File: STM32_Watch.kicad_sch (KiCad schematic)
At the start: 50 parts, among them Q1 AO3401A, SW1 SW_Push, SW2 SW_Push, U1 STM32L031K6Ux, U2 LIS2MDL, X1 32.768k

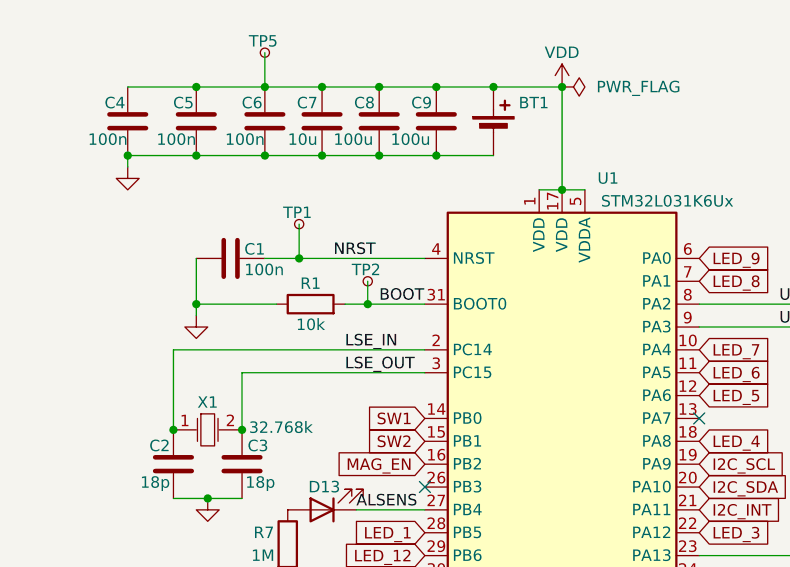
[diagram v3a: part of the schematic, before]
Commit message: Realigned components & Removed boot TP
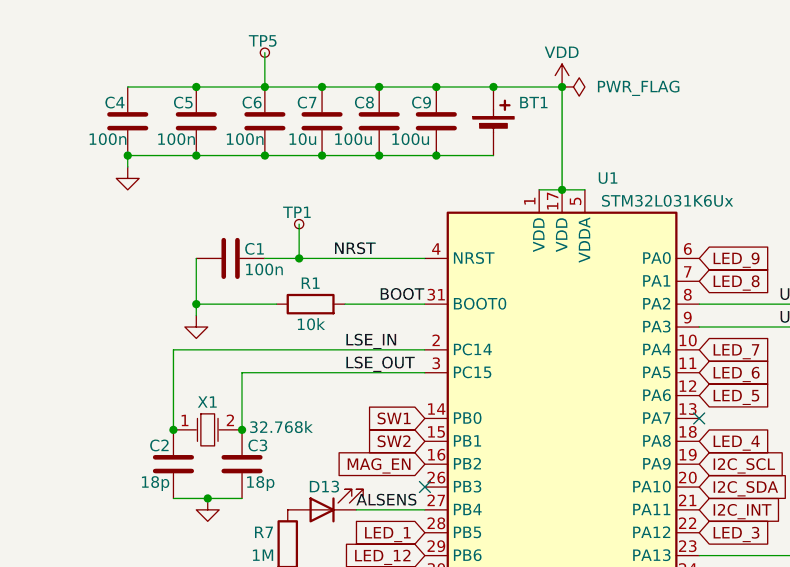
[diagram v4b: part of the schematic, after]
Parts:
- removed TP2: TestPoint_Small, TestPoint:TestPoint_Pad_D1.0mm, symbol Connector:TestPoint_Small
- TP1, TP3, TP4, TP5, TP6, TP7, TP8: footprint TestPoint:TestPoint_Pad_D1.0mm -> TestPoint:TestPoint_Pad_D1.5mm
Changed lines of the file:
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@@
 	)
 	(junction
-		(at 71.12 58.42)
-		(diameter 0)
-		(color 0 0 0 0)
-	)
-	(junction
 		(at 97.79 182.88)
 		(diameter 0)
@@
 	(wire
 		(pts
-			(xy 68.58 58.42) (xy 71.12 58.42)
-		)
-		(stroke
-			(width 0)
-			(type default)
-		)
-	)
-	(wire
-		(pts
 			(xy 101.6 154.94) (xy 106.68 154.94)
 		)
@@
 	(wire
 		(pts
-			(xy 71.12 55.88) (xy 71.12 58.42)
-		)
-		(stroke
-			(width 0)
-			(type default)
-		)
-	)
-	(wire
-		(pts
 			(xy 57.15 66.04) (xy 57.15 72.39)
 		)
@@
 	(wire
 		(pts
-			(xy 71.12 58.42) (xy 77.47 58.42)
+			(xy 68.58 58.42) (xy 77.47 58.42)
 		)
 		(stroke
@@
 			)
 		)
-		(property "Footprint" "TestPoint:TestPoint_Pad_D1.0mm"
+		(property "Footprint" "TestPoint:TestPoint_Pad_D1.5mm"
 			(at 130.81 58.42 0)
 			(effects
@@
 	)
 	(symbol
-		(lib_id "Connector:TestPoint_Small")
-		(at 71.12 55.88 0)
-		(unit 1)
-		(exclude_from_sim no)
-		(in_bom yes)
-		(on_board yes)
-		(dnp no)
-		(property "Reference" "TP2"
-			(at 69.342 54.61 0)
-			(effects
-				(font
-					(size 1.27 1.27)
-				)
-				(justify left)
-			)
-		)
-		(property "Value" "TestPoint_Small"
-			(at 72.39 57.1499 0)
-			(effects
-				(font
-					(size 1.27 1.27)
-				)
-				(justify left)
-				(hide yes)
-			)
-		)
-		(property "Footprint" "TestPoint:TestPoint_Pad_D1.0mm"
-			(at 76.2 55.88 0)
-			(effects
-				(font
-					(size 1.27 1.27)
-				)
-				(hide yes)
-			)
-		)
-		(property "Datasheet" "~"
-			(at 76.2 55.88 0)
-			(effects
-				(font
-					(size 1.27 1.27)
-				)
-				(hide yes)
-			)
-		)
-		(property "Description" "test point"
-			(at 71.12 55.88 0)
-			(effects
-				(font
-					(size 1.27 1.27)
-				)
-				(hide yes)
-			)
-		)
-		(pin "1"
-		)
-		(instances
-			(project "STM32_Watch"
-				(path "/1b502511-4b9c-43d1-bc6f-3ad66e0f6a7c"
-					(reference "TP2")
-					(unit 1)
-				)
-			)
-		)
-	)
-	(symbol
 		(lib_id "power:GND")
 		(at 92.71 101.6 0)
@@
 			)
 		)
-		(property "Footprint" "TestPoint:TestPoint_Pad_D1.0mm"
+		(property "Footprint" "TestPoint:TestPoint_Pad_D1.5mm"
 			(at 130.81 88.9 0)
 			(effects
@@
 			)
 		)
-		(property "Footprint" "TestPoint:TestPoint_Pad_D1.0mm"
+		(property "Footprint" "TestPoint:TestPoint_Pad_D1.5mm"
 			(at 130.81 86.36 0)
 			(effects
@@
 			)
 		)
-		(property "Footprint" "TestPoint:TestPoint_Pad_D1.0mm"
+		(property "Footprint" "TestPoint:TestPoint_Pad_D1.5mm"
 			(at 130.81 60.96 0)
 			(effects
@@
 			)
 		)
-		(property "Footprint" "TestPoint:TestPoint_Pad_D1.0mm"
+		(property "Footprint" "TestPoint:TestPoint_Pad_D1.5mm"
 			(at 64.77 30.48 0)
 			(effects
@@
 			)
 		)
-		(property "Footprint" "TestPoint:TestPoint_Pad_D1.0mm"
+		(property "Footprint" "TestPoint:TestPoint_Pad_D1.5mm"
 			(at 93.98 100.33 0)
 			(effects
@@
 			)
 		)
-		(property "Footprint" "TestPoint:TestPoint_Pad_D1.0mm"
+		(property "Footprint" "TestPoint:TestPoint_Pad_D1.5mm"
 			(at 68.58 49.53 0)
 			(effects

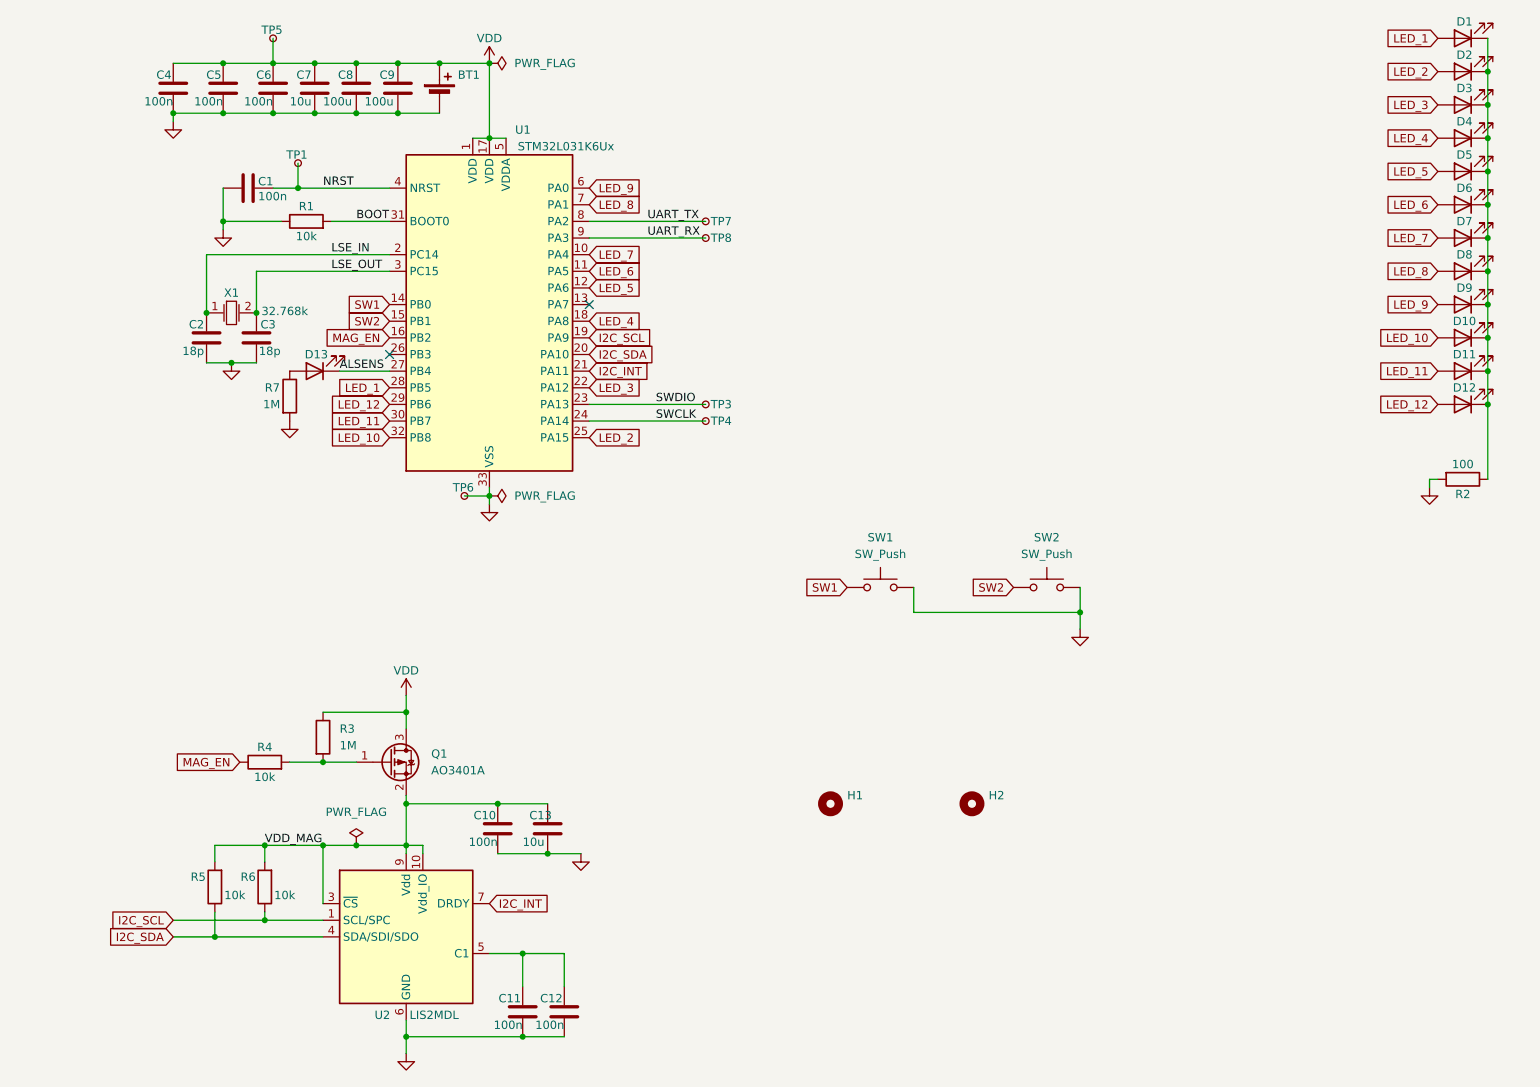
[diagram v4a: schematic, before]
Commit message: IMU instead of a compass
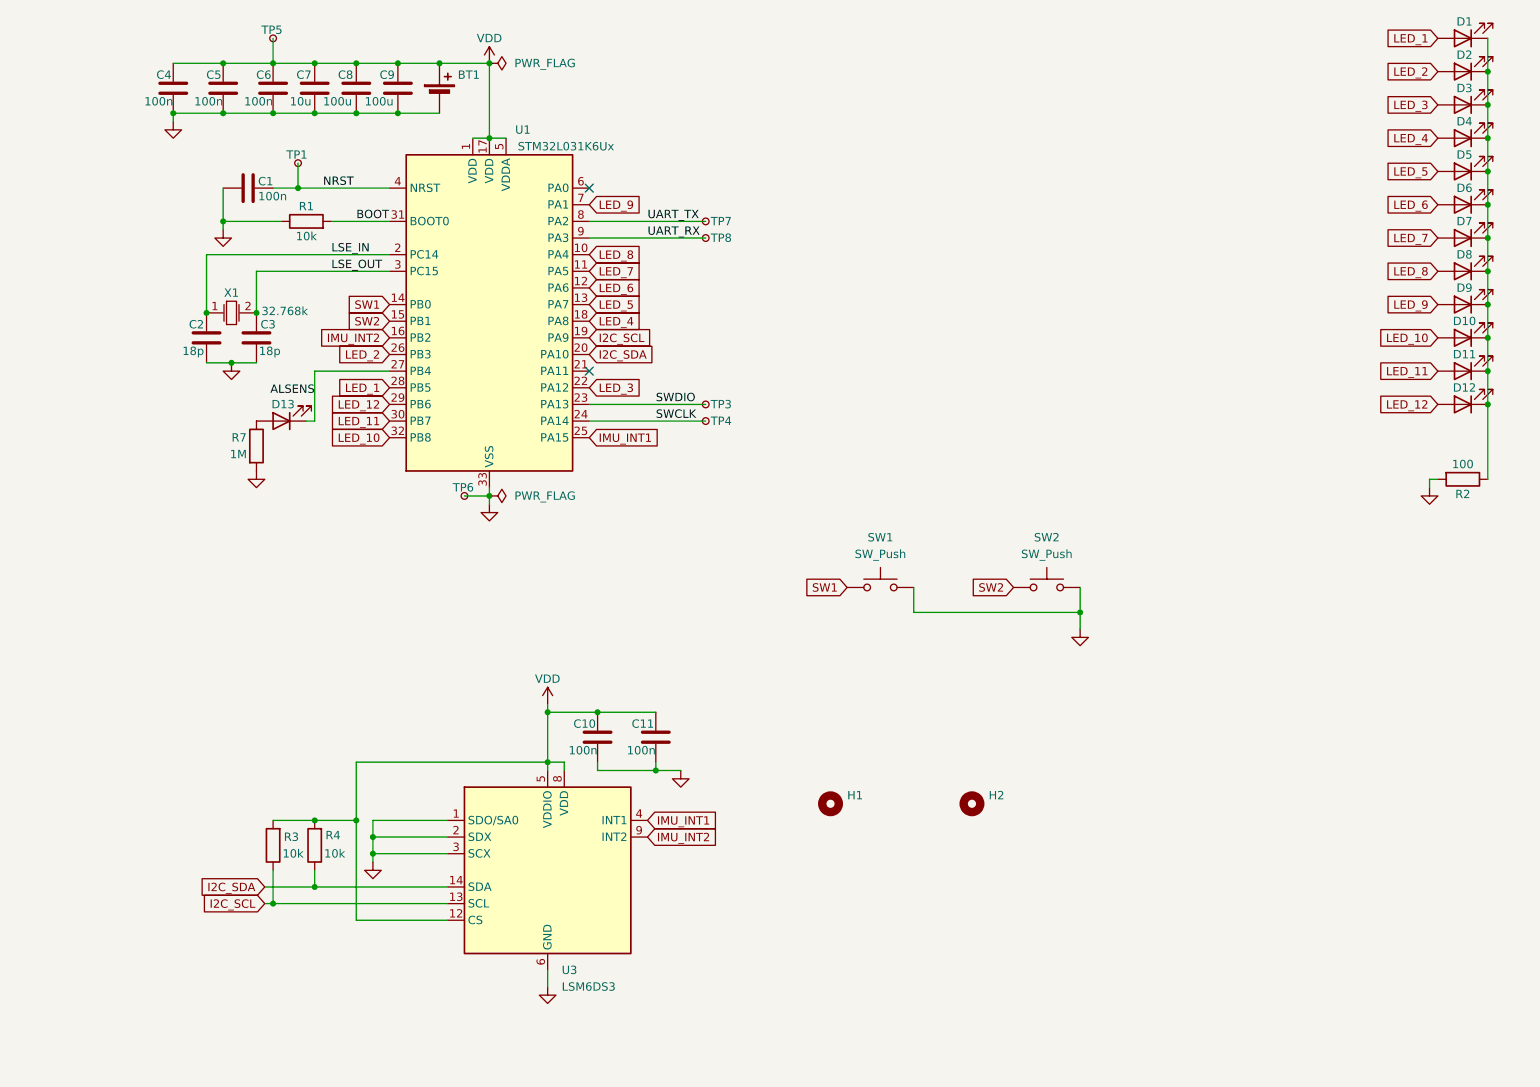
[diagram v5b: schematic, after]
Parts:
- removed C12: 100n, Capacitor_SMD:C_0603_1608Metric, symbol Device:C
- removed C13: 10u, Capacitor_SMD:C_0805_2012Metric, symbol Device:C
- removed Q1: AO3401A, Package_TO_SOT_SMD:SOT-23, symbol Transistor_FET:AO3401A
- removed R3: 1M, Resistor_SMD:R_0603_1608Metric, symbol Device:R
- removed R4: 10k, Resistor_SMD:R_0603_1608Metric, symbol Device:R
- removed U2: LIS2MDL, Package_LGA:LGA-12_2x2mm_P0.5mm, symbol Sensor_Magnetic:LIS2MDL
- added U3: LSM6DS3, Package_LGA:LGA-14_3x2.5mm_P0.5mm_LayoutBorder3x4y, symbol Sensor_Motion:LSM6DS3
- renumbered R5 to R3, R6 to R4
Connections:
- net VDD_MAG is gone; now on net VDD: C10.1, R3.2, R4.2
- net GND: now also U3.1 (SDO/SA0), U3.2 (SDX), U3.3 (SCX), U3.6 (GND), U3.7 (GND)
- net I2C_SCL: now also R3.1, U3.13 (SCL); no longer R4.1
- net I2C_SDA: now also R4.1, U3.14 (SDA); no longer R3.1
- net LED_2: now also U1.26 (PB3); no longer U1.25 (PA15)
- net LED_5: now also U1.13 (PA7); no longer U1.12 (PA6)
- net LED_6: now also U1.12 (PA6); no longer U1.11 (PA5)
- net LED_7: now also U1.11 (PA5); no longer U1.10 (PA4)
- net LED_8: now also U1.10 (PA4); no longer U1.7 (PA1)
- net LED_9: now also U1.7 (PA1); no longer U1.6 (PA0)
- net VDD: now also C11.1, U3.12 (CS), U3.5 (VDDIO), U3.8 (VDD)
- net I2C_INT: no longer names the net of U1.21 (PA11)
- net MAG_EN renamed IMU_INT2
- net IMU_INT2: now also U3.9 (INT2)
- new net IMU_INT1: U1.25 (PA15), U3.4 (INT1)
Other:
- moved on the sheet: C10, C11, D13, R3, R4, R7

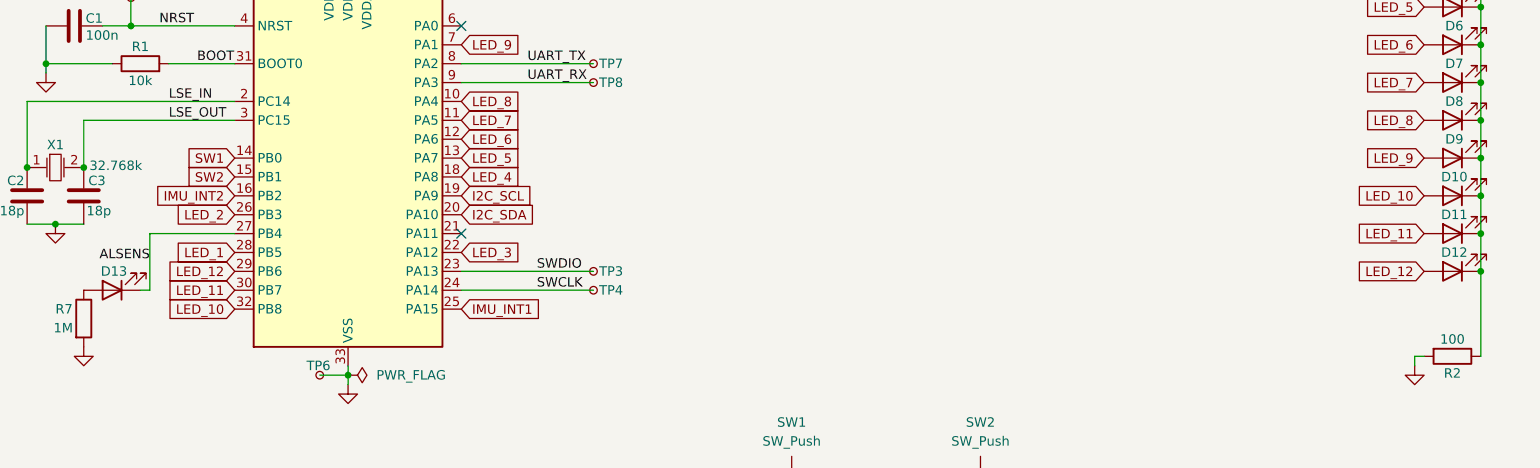
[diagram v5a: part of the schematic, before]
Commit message: Rearanged mcu pins & Routed
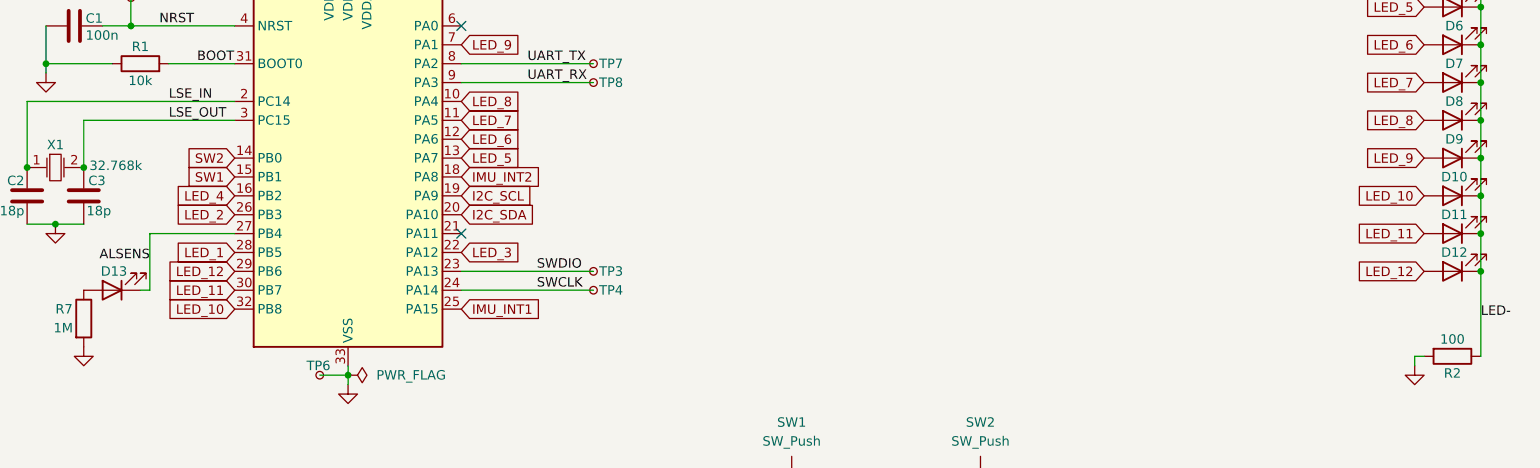
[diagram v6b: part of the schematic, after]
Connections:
- net IMU_INT2: now also U1.18 (PA8); no longer U1.16 (PB2)
- net LED_4: now also U1.16 (PB2); no longer U1.18 (PA8)
- net SW1: now also U1.15 (PB1); no longer U1.14 (PB0)
- net SW2: now also U1.14 (PB0); no longer U1.15 (PB1)
- net LED-: now reaches D1.1 (K), D10.1 (K), D11.1 (K), D12.1 (K), D2.1 (K), D3.1 (K), D4.1 (K), D5.1 (K), D6.1 (K), D7.1 (K), D8.1 (K), D9.1 (K), R2.1

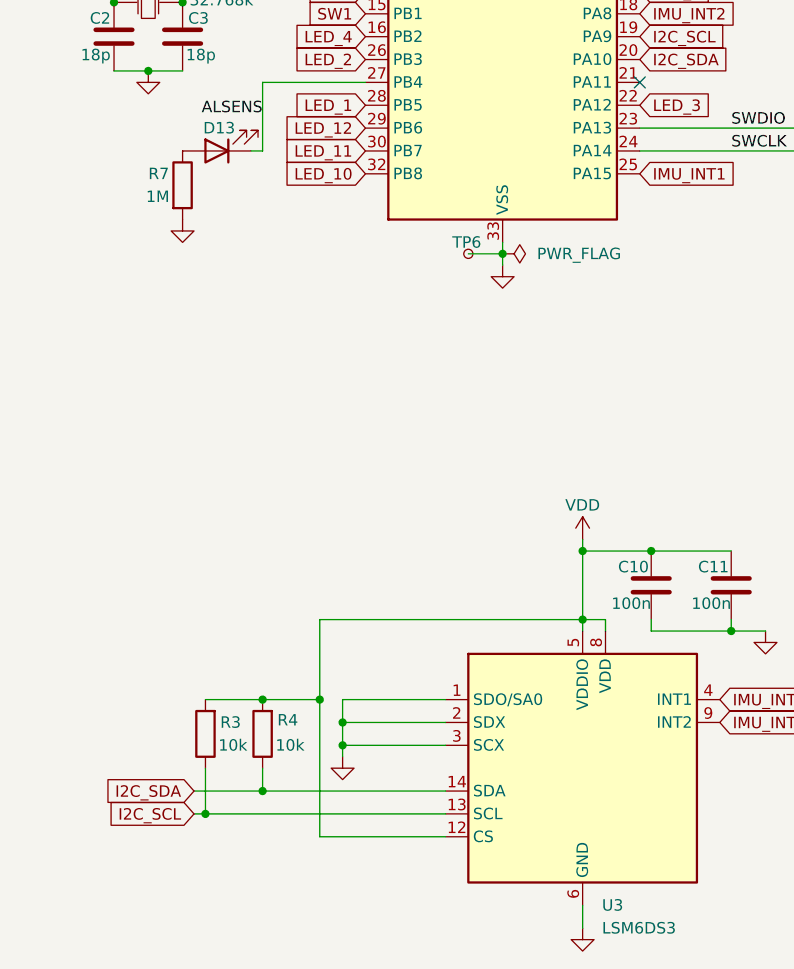
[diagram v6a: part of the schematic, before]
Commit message: Updated Routing & Fixed DRC problems
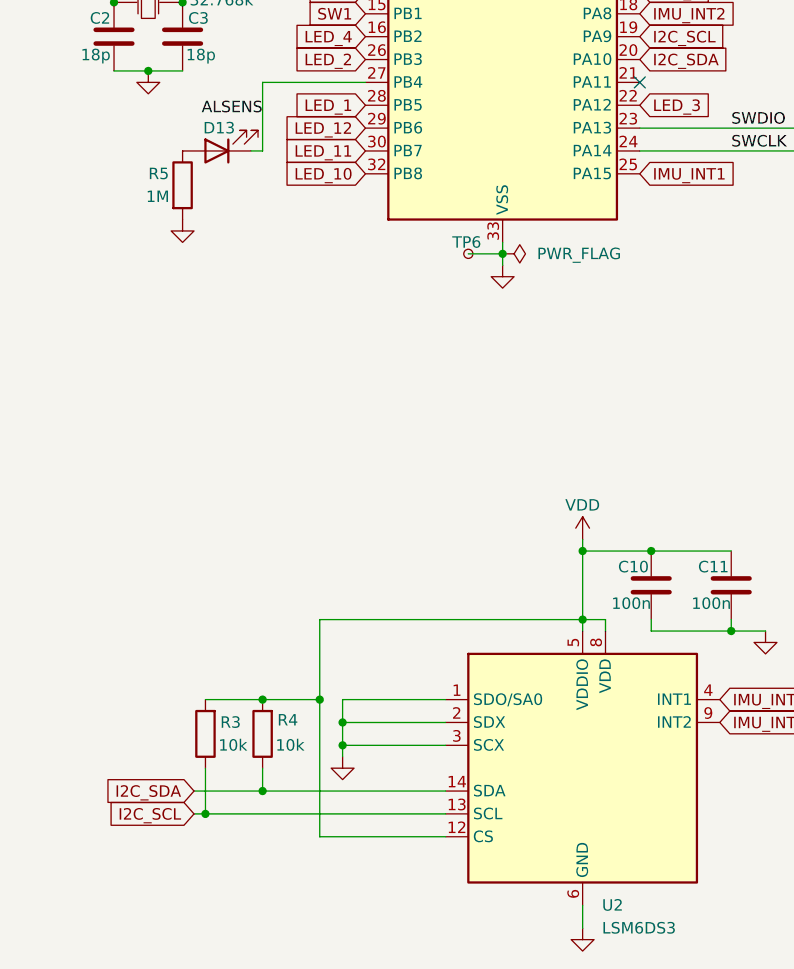
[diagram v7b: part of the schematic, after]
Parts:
- renumbered R7 to R5, U3 to U2
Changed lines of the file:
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@@
 		(dnp no)
 		(fields_autoplaced yes)
-		(property "Reference" "U3"
+		(property "Reference" "U2"
 			(at 103.7433 172.72 0)
 			(effects
@@
 			(project ""
 				(path "/1b502511-4b9c-43d1-bc6f-3ad66e0f6a7c"
-					(reference "U3")
+					(reference "U2")
 					(unit 1)
 				)
@@
 		(on_board yes)
 		(dnp no)
-		(property "Reference" "R7"
+		(property "Reference" "R5"
 			(at 53.34 91.44 0)
 			(effects
@@
 			(project "STM32_Watch"
 				(path "/1b502511-4b9c-43d1-bc6f-3ad66e0f6a7c"
-					(reference "R7")
+					(reference "R5")
 					(unit 1)
 				)
